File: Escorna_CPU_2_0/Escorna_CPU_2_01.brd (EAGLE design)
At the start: 50.2 x 85 mm, 62 parts, among them IC1 ULN2803, U2 ESP01, X1 AK550/2

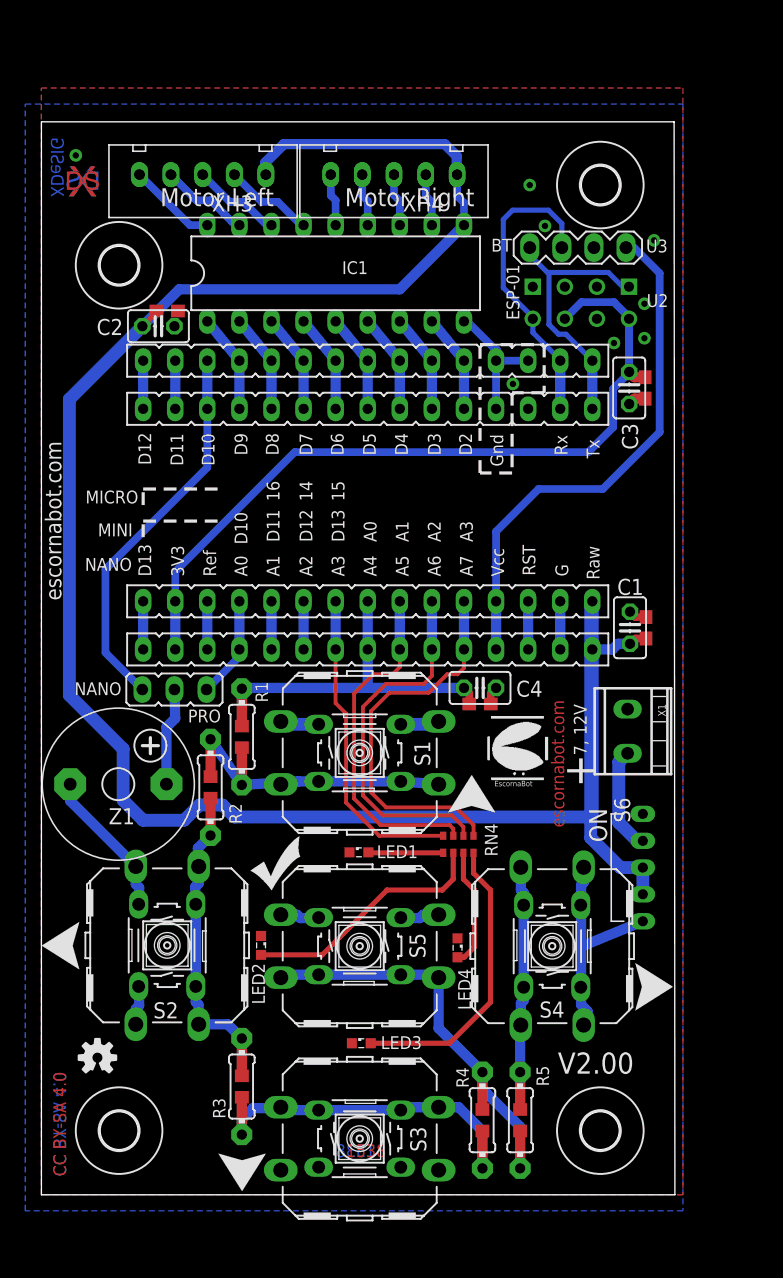
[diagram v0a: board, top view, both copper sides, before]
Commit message: error in layer top resolve
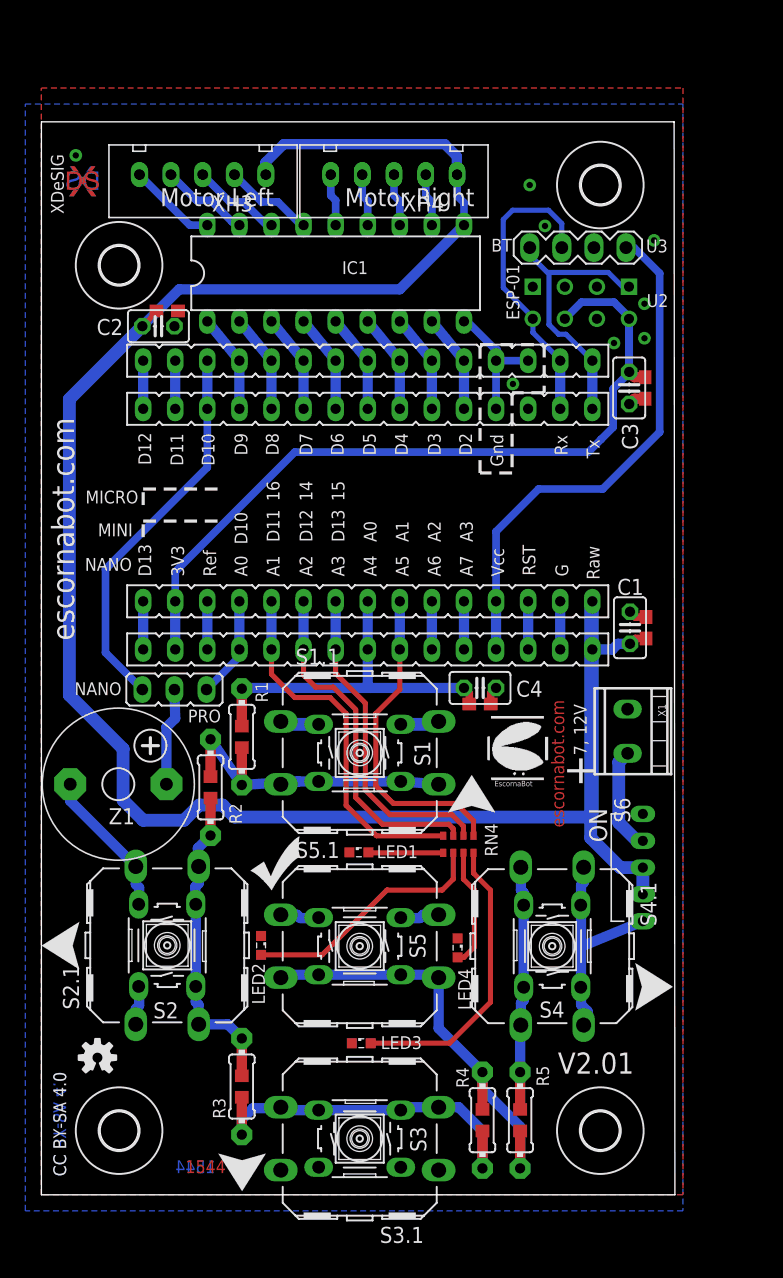
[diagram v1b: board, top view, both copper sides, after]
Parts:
- added LOGO2: OSHW-LOGOS, SparkFun-Aesthetics:OSHW-LOGO-S
- added U$1, U$11, U$3, U$6: FRECHA, escorna:FRECHA
- added U$2: GO, escorna:VALE
- C4: value 1000nF -> 10nF
- C4.1: value 100nF -> 10nF
- S1.1, S2.1, S3.1, S4.1, S5.1: device switch-omron:B3F40XX_NH -> Escorna_CPU_2_01:SWITCH-OMRON_B3F40XX_NH
- moved ESC 26.6 mm to (40.2, 32.8)
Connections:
- net A1: now also RN4.4
- net A2: now also RN4.3
- net A3: now also RN4.2; no longer RN4.4
- net A5: now also RN4.1; no longer RN4.3
- net A6: no longer RN4.2
- net A7: no longer RN4.1
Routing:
- net A7: track 30.5 -> 3.81 mm
- net A6: track 29.1 -> 3.81 mm
- net A1: track 3.81 -> 28.9 mm
- net A2: track 3.81 -> 27.4 mm
- net A5: track 27.4 -> 25.5 mm
- net RAW: track 181.3 -> 182.3 mm
- net ML3: track 7.15 -> 7.93 mm
- net A3: track 25.1 -> 25.6 mm
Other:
- board text added: "1544"
- board text added: "V2.01"
- board text removed: "1538"
- board text removed: "V2.00"

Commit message: Act S6 library
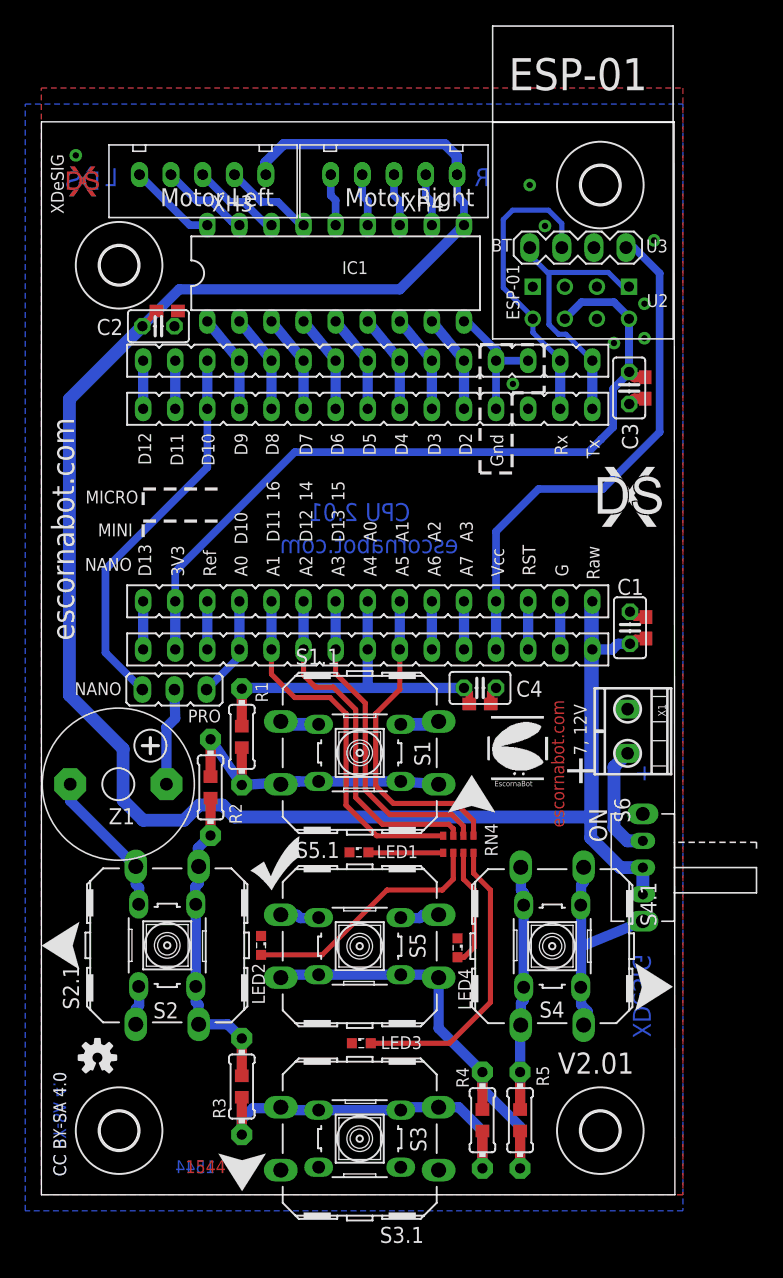
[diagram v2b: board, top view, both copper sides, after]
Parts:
- added U$12: XDESIG_XDESIG21, Escorna_CPU_2_01:XDESIG_XDESIG
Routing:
- net N$3: track 8.28 -> 9.04 mm
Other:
- board text added: "CPU 2.01"
- board text added: "L"
- board text added: "R"
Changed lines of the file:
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@@
 <grid distance="0.05" unitdist="inch" unit="mm" style="lines" multiple="1" display="no" altdistance="0.0635" altunitdist="mm" altunit="mm"/>
 <layers>
-<layer number="1" name="Top" color="1" fill="1" visible="yes" active="yes"/>
+<layer number="1" name="Top" color="1" fill="1" visible="no" active="yes"/>
 <layer number="16" name="Bottom" color="4" fill="1" visible="no" active="yes"/>
 <layer number="17" name="Pads" color="2" fill="1" visible="yes" active="yes"/>
 <layer number="18" name="Vias" color="2" fill="1" visible="yes" active="yes"/>
-<layer number="19" name="Unrouted" color="6" fill="1" visible="no" active="yes"/>
+<layer number="19" name="Unrouted" color="6" fill="1" visible="yes" active="yes"/>
 <layer number="20" name="Dimension" color="15" fill="1" visible="yes" active="yes"/>
-<layer number="21" name="tPlace" color="7" fill="1" visible="no" active="yes"/>
+<layer number="21" name="tPlace" color="7" fill="1" visible="yes" active="yes"/>
 <layer number="22" name="bPlace" color="7" fill="1" visible="no" active="yes"/>
 <layer number="23" name="tOrigins" color="15" fill="1" visible="no" active="yes"/>
@@
 <text x="1.778" y="77.6605" size="1.016" layer="21" font="vector" ratio="10" distance="60" rot="R90">XDeSIG</text>
 <text x="1.016" y="1.4605" size="1.016" layer="22" font="vector" rot="MR90">CC BY-SA 4.0</text>
+<text x="33.02" y="50.8" size="1.4224" layer="16" font="vector" rot="MR0">escornabot.com</text>
+<text x="29.21" y="53.34" size="1.4224" layer="16" font="vector" rot="MR0">CPU 2.01</text>
+<text x="48.26" y="19.05" size="1.4224" layer="16" font="vector" rot="MR270">XDeSIG</text>
+<text x="48.5775" y="34.0995" size="1.4224" layer="16" font="vector" rot="MR270">+</text>
+<text x="34.29" y="81.28" size="1.4224" layer="16" font="vector" rot="MR180">R</text>
+<text x="5.08" y="81.28" size="1.4224" layer="16" font="vector" rot="MR180">L</text>
 </plain>
 <attributes>
@@
 <element name="U$6" library="escorna" package="FRECHA" value="FRECHA" x="17.78" y="3.302" rot="MR270"/>
 <element name="U$11" library="escorna" package="FRECHA" value="FRECHA" x="32.131" y="30.1625" rot="MR90"/>
+<element name="U$12" library="Escorna_CPU_2_01" package="XDESIG_XDESIG" value="XDESIG_XDESIG21" x="44.069" y="52.8955"/>
 </elements>
 <signals>
@@
 <wire x1="2.286" y1="32.512" x2="2.286" y2="31.1912" width="0.8128" layer="16"/>
 <wire x1="2.286" y1="31.1912" x2="7.4803" y2="25.9969" width="0.8128" layer="16"/>
-<polygon width="0.3048" layer="16">
+<polygon width="0.3048" layer="16" isolate="0.4064">
 <vertex x="-1.27" y="86.36"/>
 <vertex x="50.8" y="86.36"/>
@@
 <contactref element="S6" pad="P$2"/>
 <contactref element="X1" pad="1"/>
-<wire x1="47.625" y1="28.023" x2="47.161" y2="28.023" width="1.016" layer="16"/>
-<wire x1="47.161" y1="28.023" x2="45.72" y2="29.464" width="1.016" layer="16"/>
-<wire x1="45.72" y1="29.464" x2="45.72" y2="34.2545" width="1.016" layer="16"/>
-<wire x1="45.72" y1="34.2545" x2="46.4185" y2="34.953" width="1.016" layer="16"/>
+<wire x1="47.625" y1="28.023" x2="46.399" y2="28.023" width="1.016" layer="16"/>
+<wire x1="46.399" y1="28.023" x2="45.339" y2="29.083" width="1.016" layer="16"/>
+<wire x1="45.339" y1="29.083" x2="45.339" y2="33.8735" width="1.016" layer="16"/>
+<wire x1="45.339" y1="33.8735" x2="46.4185" y2="34.953" width="1.016" layer="16"/>
 </signal>
 <signal name="S5">
